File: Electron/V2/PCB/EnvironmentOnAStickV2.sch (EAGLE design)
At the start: 15 parts, among them U1 HTU21DSMD, U2 BMP180, U4 LIGHTSENSORTEMT6000

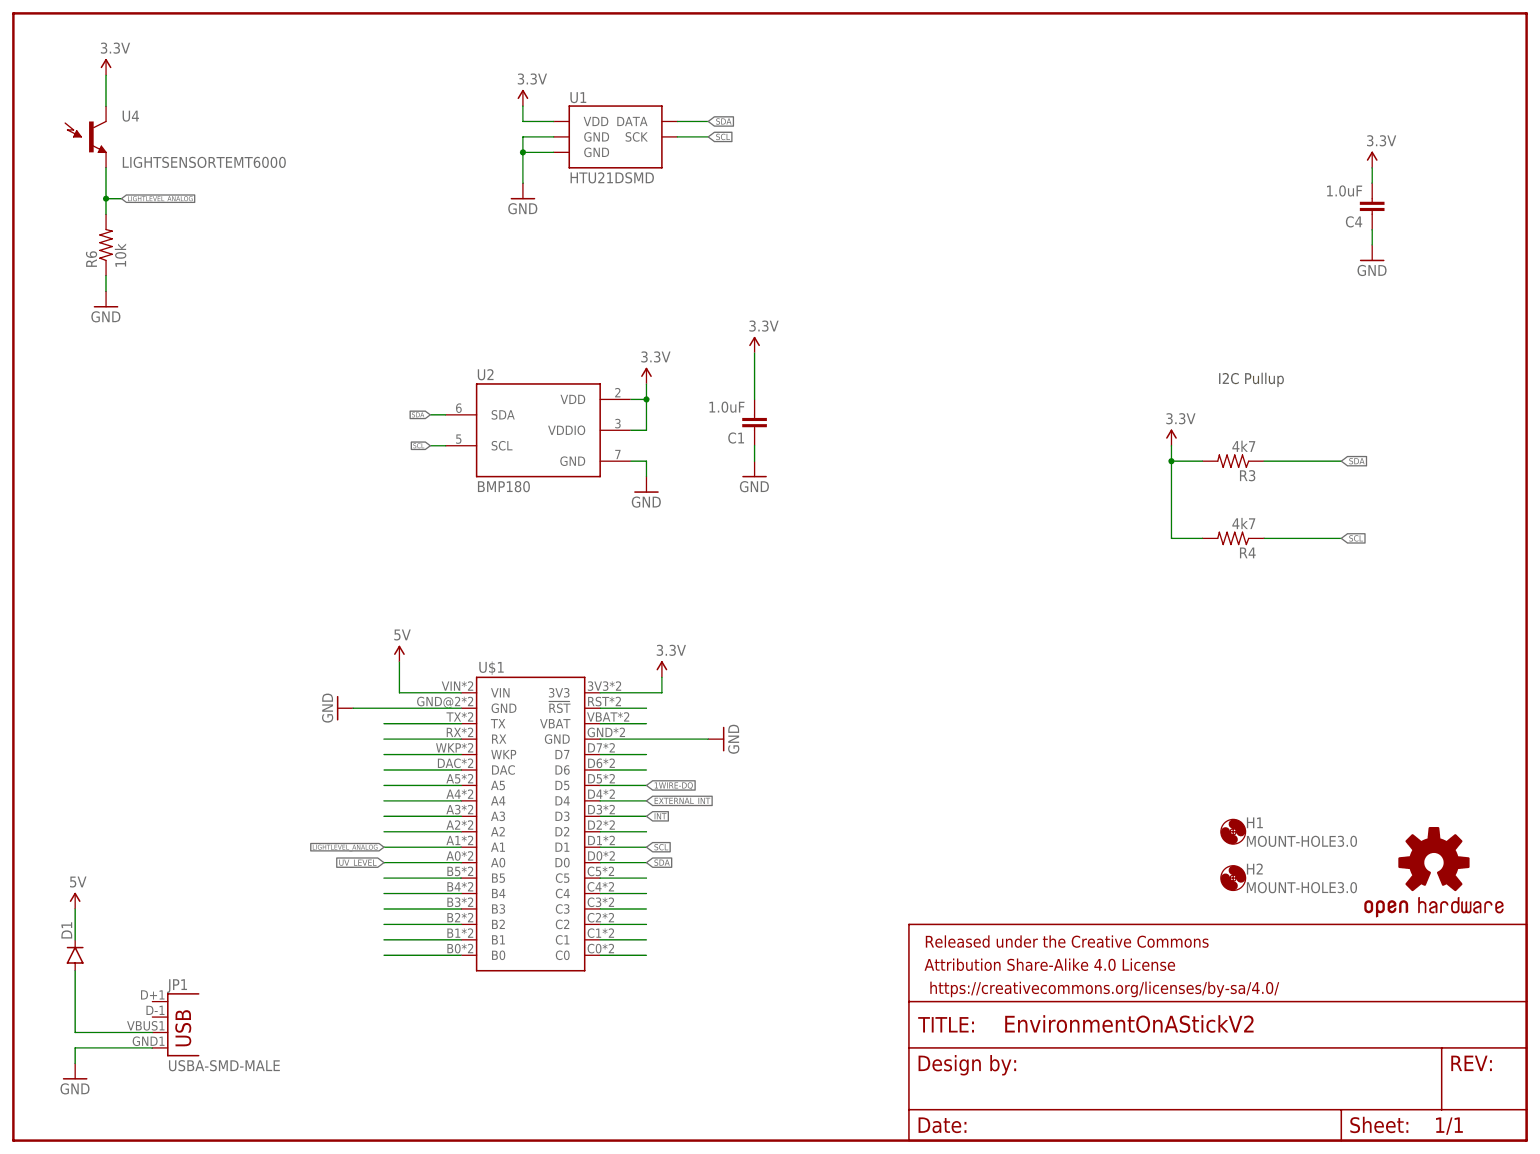
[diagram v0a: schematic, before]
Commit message: Added reverse mount LED to V2 environment stick and moved OSH logo to cover it.
Exported PCB/schema to pdf and images.

Added datasheet for BMP180
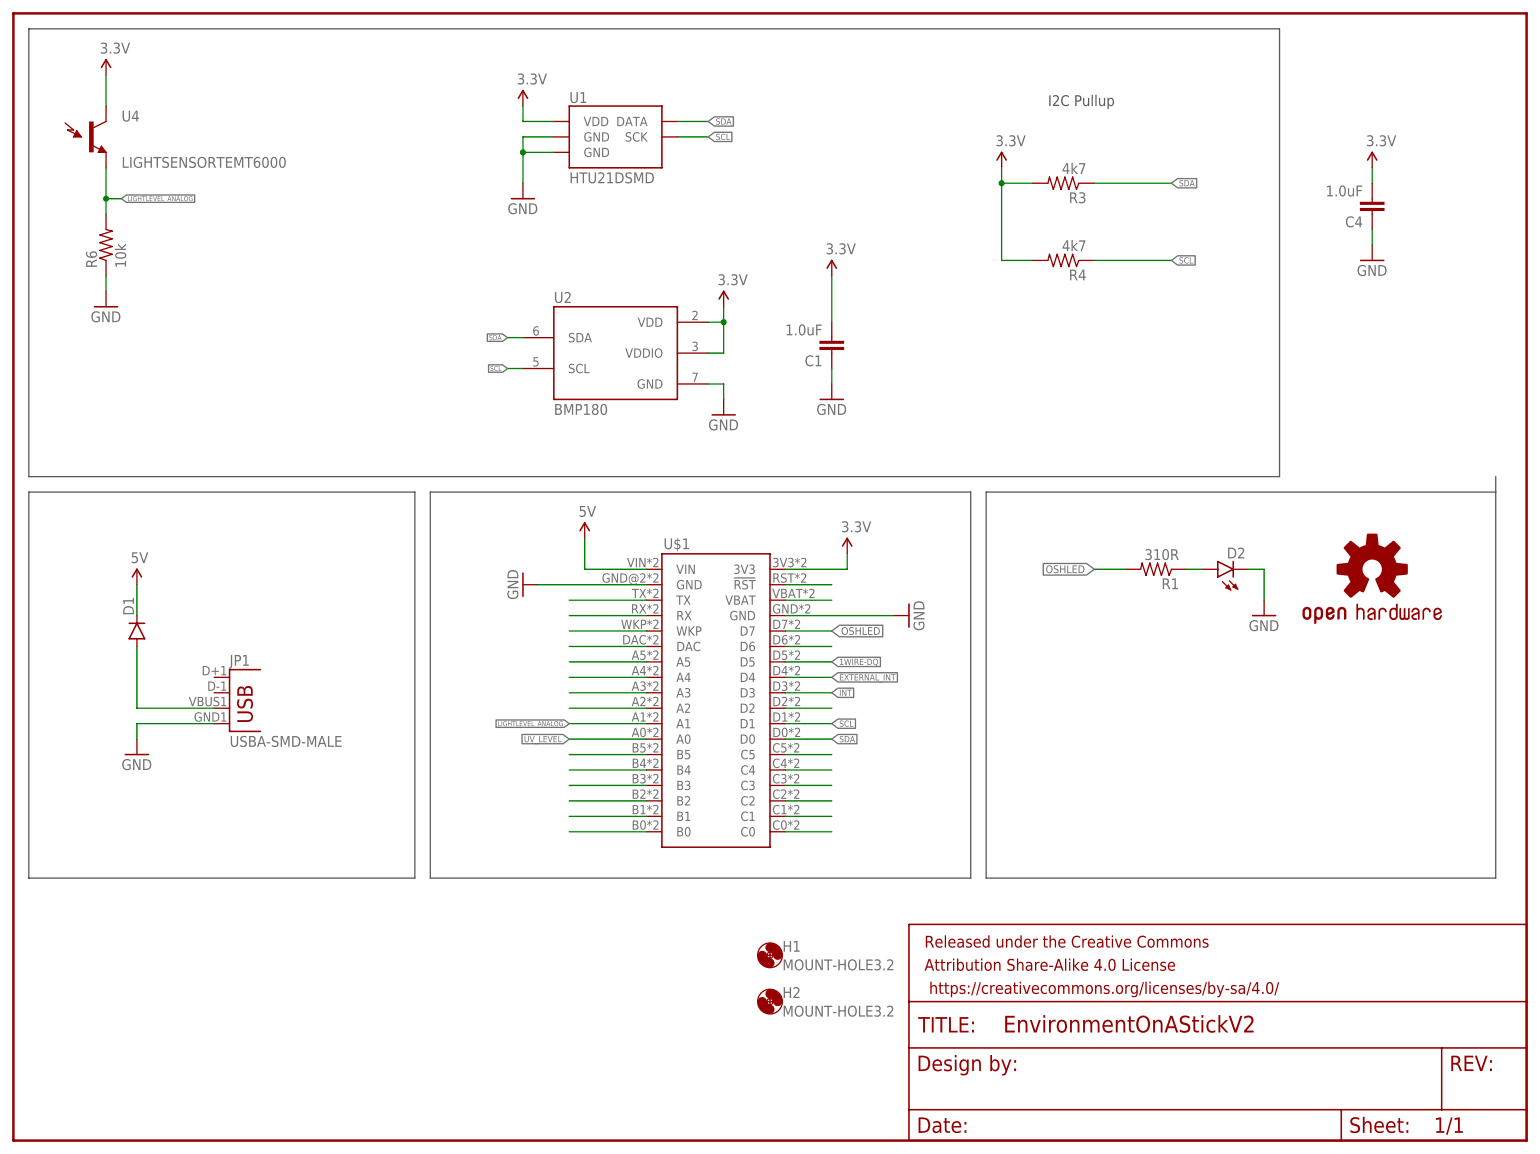
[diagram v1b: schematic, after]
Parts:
- added D2: (no value), SparkFun-LED:LED1206-BOTTOM
- added R1: 310R, SparkFun-Resistors:RESISTOR0805-RES
- H1, H2: value MOUNT-HOLE3.0 -> MOUNT-HOLE3.2; device holes:MOUNT-HOLE3.0 -> holes:MOUNT-HOLE3.2
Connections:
- removed net N$3: U$1.D7
- new net N$6: D2.A, R1.1
- new net OSHLED: R1.2, U$1.D7
- net GND: now also D2.C
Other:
- moved on the sheet: C1, D1, H1, H2, JP1, R3, R4, U$1, U2
